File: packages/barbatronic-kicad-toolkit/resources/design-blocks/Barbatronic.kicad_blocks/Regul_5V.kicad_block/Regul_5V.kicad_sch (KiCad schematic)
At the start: 4 parts, among them U1 AMS1117-3.3

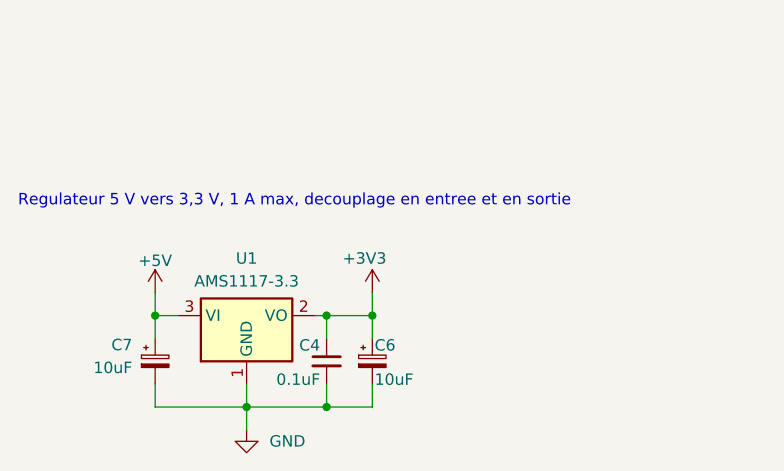
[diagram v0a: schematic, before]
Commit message: Sync docs with hand-edited design blocks
Entree_Alim_Protegee is gone, Servos_x4 is now the reusable single-
output Servos, and Regul_5V is new (78E05, needs the SparkFun PCM
power-symbols package for one symbol). Blocks are now maintained by
hand in KiCad, not generated.

Guard make_design_blocks.py behind --force: it wipes and rebuilds
the whole block library from a now-stale list, which would have
silently destroyed these edits on next run.
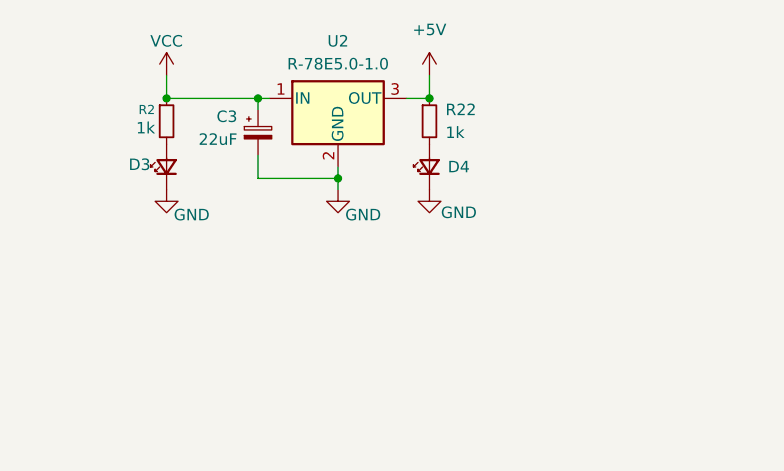
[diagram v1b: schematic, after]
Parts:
- removed C4: 0.1uF, Capacitor_SMD:C_1206_3216Metric_Pad1.33x1.80mm_HandSolder, symbol Device:C_Small
- removed C6, C7: 10uF, Capacitor_SMD:CP_Elec_5x5.4, symbol Device:C_Polarized_Small
- removed U1: AMS1117-3.3, Package_TO_SOT_SMD:SOT-223-3_TabPin2, symbol Regulator_Linear:AMS1117-3.3
- added C3: 22uF, Capacitor_SMD:CP_Elec_5x5.4, symbol Device:C_Polarized_Small
- added D3, D4: LED_Small, LED_SMD:LED_1206_3216Metric_Pad1.42x1.75mm_HandSolder, symbol Device:LED_Small
- added R2, R22: 1k, Resistor_SMD:R_1206_3216Metric_Pad1.30x1.75mm_HandSolder, symbol Device:R_Small
- added U2: R-78E5.0-1.0, Converter_DCDC:Converter_DCDC_RECOM_R-78E-0.5_THT, symbol Converter_DCDC:R-78E5.0-1.0
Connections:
- net +5V: now also R22.1, U2.3 (OUT)
- net GND: now also C3.2, D3.1 (K), D4.1 (K), U2.2 (GND)
- new net: D4.2 (A), R22.2
- new net: D3.2 (A), R2.2
- new net VCC: C3.1, R2.1, U2.1 (IN)
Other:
- note removed: "Regulateur 5 V vers 3,3 V, 1 A max, decouplage en entree et en sortie"
